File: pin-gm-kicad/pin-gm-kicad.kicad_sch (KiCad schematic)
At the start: 37 parts

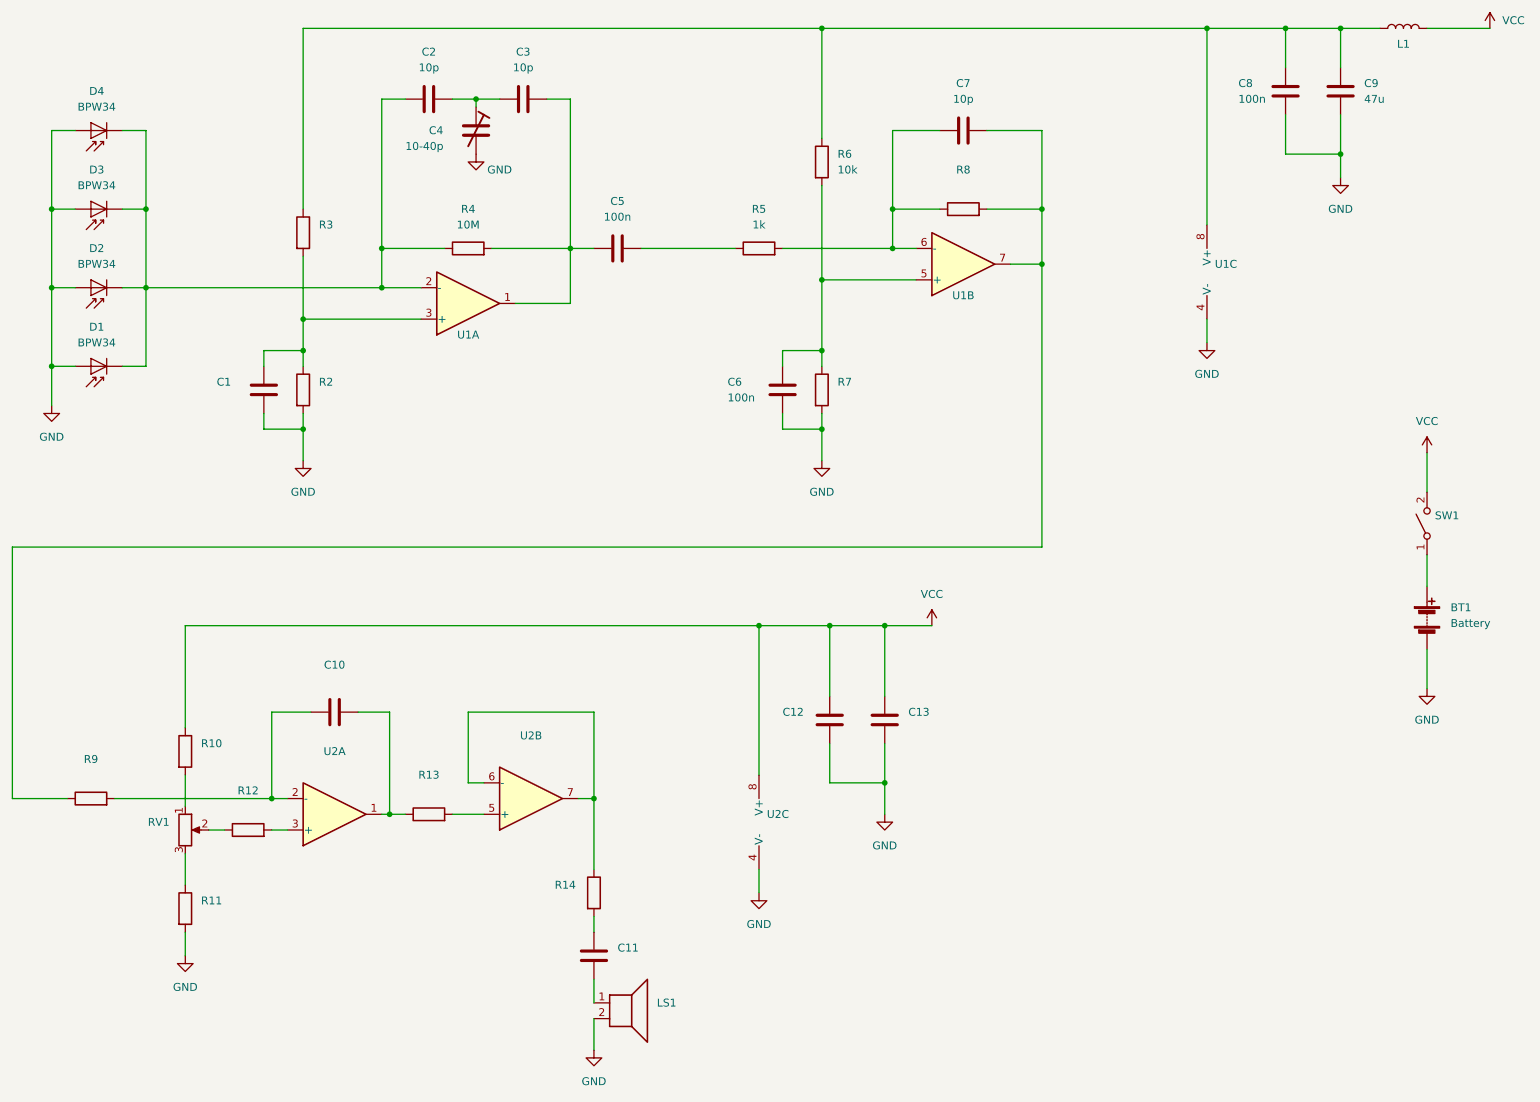
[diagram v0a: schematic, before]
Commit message: trimmer kondi footprint kezdemény
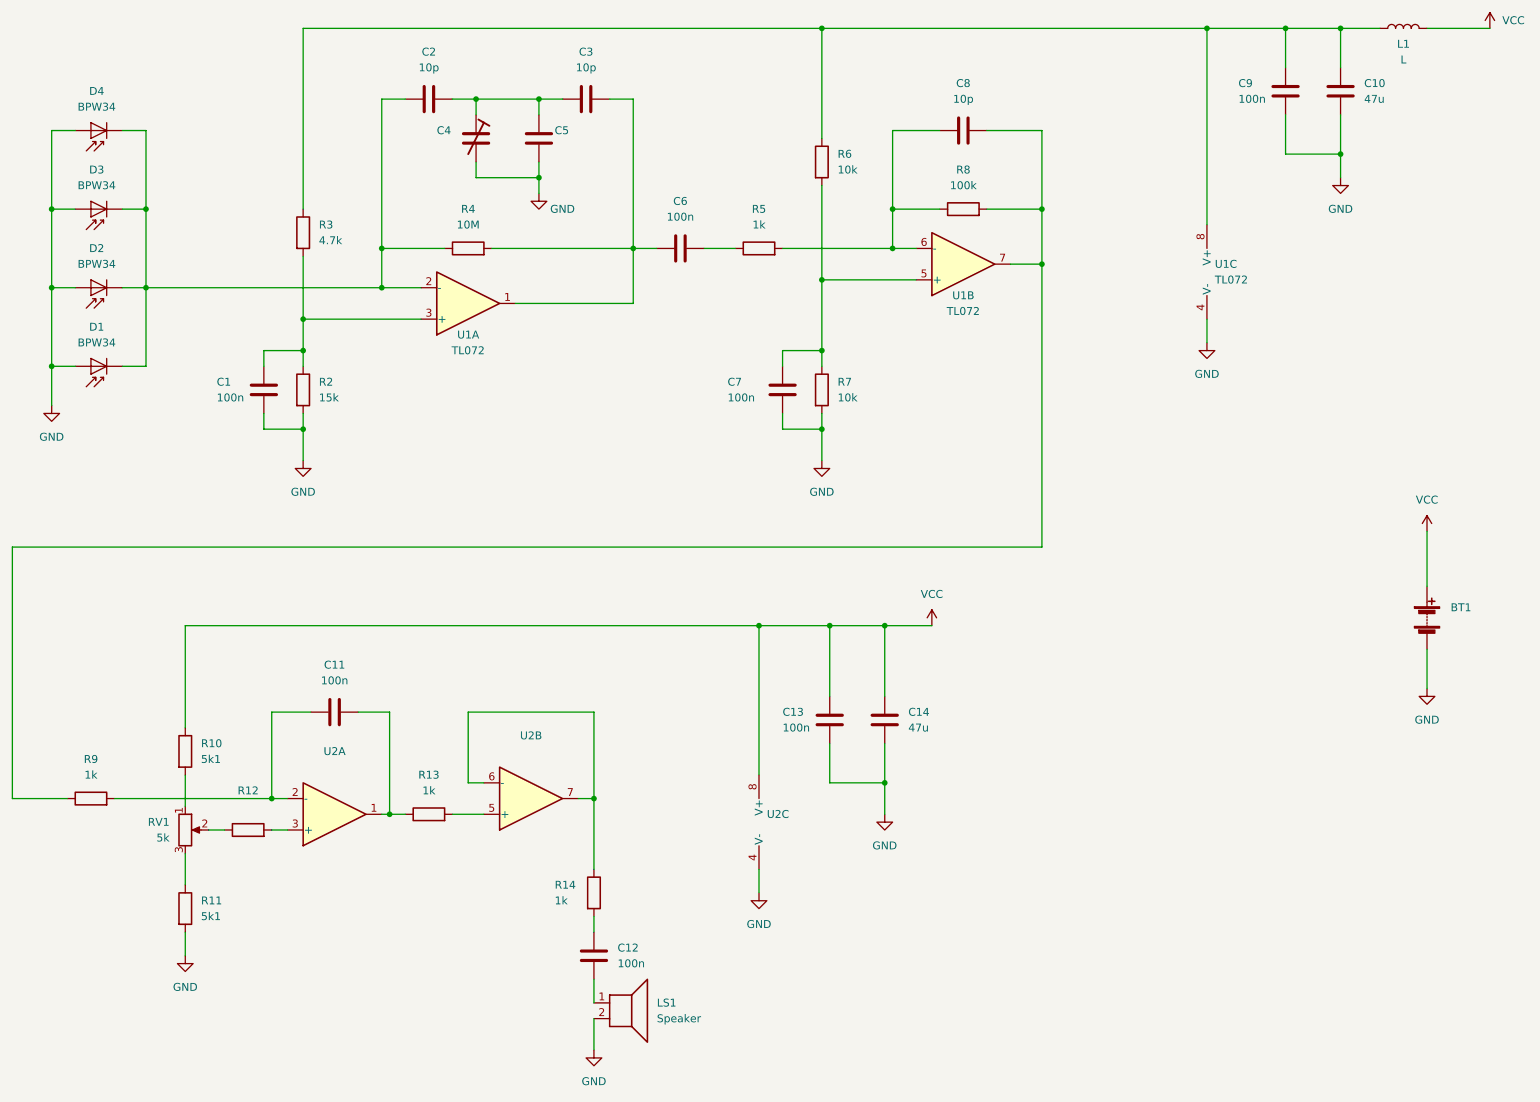
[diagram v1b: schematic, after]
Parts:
- removed SW1: (no value), symbol Switch:SW_SPST
- added C5: (no value), symbol Device:C
- BT1: value Battery -> (none)
- C1: value (none) -> 100n; footprint (none) -> Capacitor_SMD:C_1206_3216Metric_Pad1.33x1.80mm_HandSolder
- C10: renamed from C9; footprint (none) -> Capacitor_SMD:C_1210_3225Metric_Pad1.33x2.70mm_HandSolder
- C11: renamed from C10; value (none) -> 100n; footprint (none) -> Capacitor_SMD:C_1206_3216Metric_Pad1.33x1.80mm_HandSolder
- C12: renamed from C11; value (none) -> 100n; footprint (none) -> Capacitor_SMD:C_1206_3216Metric_Pad1.33x1.80mm_HandSolder
- C13: renamed from C12; value (none) -> 100n; footprint (none) -> Capacitor_SMD:C_1206_3216Metric_Pad1.33x1.80mm_HandSolder
- C14: renamed from C13; value (none) -> 47u; footprint (none) -> Capacitor_SMD:C_1210_3225Metric_Pad1.33x2.70mm_HandSolder
- C2, C3: footprint (none) -> Capacitor_SMD:C_1206_3216Metric_Pad1.33x1.80mm_HandSolder
- C4: value 10-40p -> (none)
- C6: renamed from C5; footprint (none) -> Capacitor_SMD:C_1206_3216Metric_Pad1.33x1.80mm_HandSolder
- C7: renamed from C6; footprint (none) -> Capacitor_SMD:C_1206_3216Metric_Pad1.33x1.80mm_HandSolder
- C8: renamed from C7; footprint (none) -> Capacitor_SMD:C_1206_3216Metric_Pad1.33x1.80mm_HandSolder
- C9: renamed from C8; footprint (none) -> Capacitor_SMD:C_1206_3216Metric_Pad1.33x1.80mm_HandSolder
- L1: value (none) -> L; footprint (none) -> Inductor_SMD:L_Bourns_SRR0604_homemade
- LS1: value (none) -> Speaker; footprint (none) -> Connector_Wire:SolderWire-2sqmm_1x02_P7.8mm_D2mm_OD3.9mm
- R10, R11: value (none) -> 5k1; footprint (none) -> Resistor_SMD:R_1206_3216Metric_Pad1.30x1.75mm_HandSolder
- R13, R9: value (none) -> 1k; footprint (none) -> Resistor_SMD:R_1206_3216Metric_Pad1.30x1.75mm_HandSolder
- R14: value (none) -> 1k; footprint (none) -> Resistor_SMD:R_1206_3216Metric
- R2: value (none) -> 15k; footprint (none) -> Resistor_SMD:R_1206_3216Metric_Pad1.30x1.75mm_HandSolder
- R3: value (none) -> 4.7k; footprint (none) -> Resistor_SMD:R_1206_3216Metric_Pad1.30x1.75mm_HandSolder
- R4, R5, R6: footprint (none) -> Resistor_SMD:R_1206_3216Metric_Pad1.30x1.75mm_HandSolder
- R7: value (none) -> 10k; footprint (none) -> Resistor_SMD:R_1206_3216Metric_Pad1.30x1.75mm_HandSolder
- R8: value (none) -> 100k; footprint (none) -> Resistor_SMD:R_1206_3216Metric_Pad1.30x1.75mm_HandSolder
- RV1: value (none) -> 5k; footprint (none) -> Potentiometer_THT:Potentiometer_Piher_PT-10-V10_Vertical
- U1: value (none) -> TL072; footprint (none) -> Package_SO:SO-8_3.9x4.9mm_P1.27mm
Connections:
- net GND: now also C5.2
- net VCC: now also BT1.1 (+)
- net at C2.2, C3.1, C4.1: now also C5.1
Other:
- moved on the sheet: C3, C4, C6

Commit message: kb semmi
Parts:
- C1: value 100n -> (none); footprint Capacitor_SMD:C_1206_3216Metric_Pad1.33x1.80mm_HandSolder -> (none)
- C10: renamed from C13; value 100n -> (none); footprint Capacitor_SMD:C_1206_3216Metric_Pad1.33x1.80mm_HandSolder -> (none)
- C11: renamed from C14; value 47u -> (none); footprint Capacitor_SMD:C_1210_3225Metric_Pad1.33x2.70mm_HandSolder -> (none)
- C12: renamed from C8; value 10p -> (none); footprint Capacitor_SMD:C_1206_3216Metric_Pad1.33x1.80mm_HandSolder -> (none)
- C13: renamed from C9; value 100n -> (none); footprint Capacitor_SMD:C_1206_3216Metric_Pad1.33x1.80mm_HandSolder -> (none)
- C14: renamed from C10; value 47u -> (none); footprint Capacitor_SMD:C_1210_3225Metric_Pad1.33x2.70mm_HandSolder -> (none)
- C2: renamed from C11; value 100n -> (none); footprint Capacitor_SMD:C_1206_3216Metric_Pad1.33x1.80mm_HandSolder -> (none)
- C3: renamed from C2; value 10p -> (none); footprint Capacitor_SMD:C_1206_3216Metric_Pad1.33x1.80mm_HandSolder -> (none)
- C6: renamed from C3; value 10p -> (none); footprint Capacitor_SMD:C_1206_3216Metric_Pad1.33x1.80mm_HandSolder -> (none)
- C7: renamed from C12; value 100n -> (none); footprint Capacitor_SMD:C_1206_3216Metric_Pad1.33x1.80mm_HandSolder -> (none)
- C8: renamed from C6; value 100n -> (none); footprint Capacitor_SMD:C_1206_3216Metric_Pad1.33x1.80mm_HandSolder -> (none)
- C9: renamed from C7; value 100n -> (none); footprint Capacitor_SMD:C_1206_3216Metric_Pad1.33x1.80mm_HandSolder -> (none)
- D1: renamed from D4; value BPW34 -> (none); footprint OptoDevice:Osram_DIL2_4.3x4.65mm_P5.08mm -> (none)
- D2: renamed from D3; value BPW34 -> (none); footprint OptoDevice:Osram_DIL2_4.3x4.65mm_P5.08mm -> (none)
- D3: renamed from D2; value BPW34 -> (none); footprint OptoDevice:Osram_DIL2_4.3x4.65mm_P5.08mm -> (none)
- D4: renamed from D1; value BPW34 -> (none); footprint OptoDevice:Osram_DIL2_4.3x4.65mm_P5.08mm -> (none)
- L1: value L -> (none); footprint Inductor_SMD:L_Bourns_SRR0604_homemade -> (none)
- LS1: value Speaker -> (none); footprint Connector_Wire:SolderWire-2sqmm_1x02_P7.8mm_D2mm_OD3.9mm -> (none)
- R1: renamed from R9; value 1k -> (none); footprint Resistor_SMD:R_1206_3216Metric_Pad1.30x1.75mm_HandSolder -> (none)
- R10: renamed from R5; value 1k -> (none); footprint Resistor_SMD:R_1206_3216Metric_Pad1.30x1.75mm_HandSolder -> (none)
- R11: renamed from R6; value 10k -> (none); footprint Resistor_SMD:R_1206_3216Metric_Pad1.30x1.75mm_HandSolder -> (none)
- R12: renamed from R7; value 10k -> (none); footprint Resistor_SMD:R_1206_3216Metric_Pad1.30x1.75mm_HandSolder -> (none)
- R13: renamed from R8; value 100k -> (none); footprint Resistor_SMD:R_1206_3216Metric_Pad1.30x1.75mm_HandSolder -> (none)
- R2: renamed from R10; value 5k1 -> (none); footprint Resistor_SMD:R_1206_3216Metric_Pad1.30x1.75mm_HandSolder -> (none)
- R3: renamed from R11; value 5k1 -> (none); footprint Resistor_SMD:R_1206_3216Metric_Pad1.30x1.75mm_HandSolder -> (none)
- R5: renamed from R3; value 4.7k -> (none); footprint Resistor_SMD:R_1206_3216Metric_Pad1.30x1.75mm_HandSolder -> (none)
- R6: renamed from R2; value 15k -> (none); footprint Resistor_SMD:R_1206_3216Metric_Pad1.30x1.75mm_HandSolder -> (none)
- R7: renamed from R13; value 1k -> (none); footprint Resistor_SMD:R_1206_3216Metric_Pad1.30x1.75mm_HandSolder -> (none)
- R8: renamed from R4; value 10M -> (none); footprint Resistor_SMD:R_1206_3216Metric_Pad1.30x1.75mm_HandSolder -> (none)
- R9: renamed from R14; value 1k -> (none); footprint Resistor_SMD:R_1206_3216Metric -> (none)
- RV1: value 5k -> (none); footprint Potentiometer_THT:Potentiometer_Piher_PT-10-V10_Vertical -> (none)
- U2: renamed from U1; value TL072 -> (none); footprint Package_SO:SO-8_3.9x4.9mm_P1.27mm -> (none)
- renumbered R12 to R4, U2 to U1

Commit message: kész vannak a footprintek
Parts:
- added C7: (no value), symbol Device:C
- renumbered C9 to C10, C10 to C11, C11 to C12, C12 to C13, C13 to C14, C14 to C15, C7 to C6, C6 to C8, C8 to C9
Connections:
- net GND: now also C7.2
- net at C8.2, C9.1: no longer R8.2, U2.1
- net Diode_Cathode: now reaches C3.1, D1.1 (K), D2.1 (K), D3.1 (K), D4.1 (K), R8.1, U2.2 (-)
- net at C3.2, C4.1, C5.1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: now also C7.1
- new net: R8.2, U2.1
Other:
- moved on the sheet: C8, C9, R10

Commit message: kis haladás
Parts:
- BT1: value (none) -> Battery; footprint (none) -> Homemade:SolderWire-homemade
- C1, C10, C11, C14, C2, C6, C9: value (none) -> 100n; footprint (none) -> Homemade:C_1206_3216Metric_homemade
- C12, C15: value (none) -> 47u; footprint (none) -> Homemade:C_1210_3225Metric_homemade
- C13, C3, C5, C7, C8: value (none) -> 10p; footprint (none) -> Homemade:C_1206_3216Metric_homemade
- C4: value (none) -> 10-40p; footprint (none) -> Homemade:C_trimmer_D10mm_homemade
- D1, D2, D4: value (none) -> BPW34; footprint (none) -> Homemade:BPW34_homemade
- L1: value (none) -> 1m; footprint (none) -> Homemade:L_Bourns_SRR0604_homemade
- LS1: value (none) -> Speaker; footprint (none) -> Homemade:SolderWire-homemade
- R1, R10, R4, R7, R9: value (none) -> 1k; footprint (none) -> Homemade:R_1206_3216Metric_homemade
- R11, R12: value (none) -> 10k; footprint (none) -> Homemade:R_1206_3216Metric_homemade
- R13: value (none) -> 100k; footprint (none) -> Homemade:R_1206_3216Metric_homemade
- R2, R3: value (none) -> 5k1; footprint (none) -> Homemade:R_1206_3216Metric_homemade
- R5: value (none) -> 4.7k; footprint (none) -> Homemade:R_1206_3216Metric_homemade
- R6: value (none) -> 15k; footprint (none) -> Homemade:R_1206_3216Metric_homemade
- R8: value (none) -> 10M; footprint (none) -> Homemade:R_1206_3216Metric_homemade
- RV1: value (none) -> 5k; footprint (none) -> Homemade:Potentiometer_D10_vert_homemade
- U1: value (none) -> LM358; footprint (none) -> Homemade:SO-8_3.9x4.9mm_homemade
- U2: value (none) -> TL072; footprint (none) -> Homemade:SO-8_3.9x4.9mm_homemade

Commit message: kb elhelyezve
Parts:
- added H1, H2: (no value), symbol Mechanical:MountingHole_Pad
- BT1: value Battery -> (none); footprint Homemade:SolderWire-homemade -> (none)
- C1, C10, C11, C14, C2, C6, C9: value 100n -> (none); footprint Homemade:C_1206_3216Metric_homemade -> (none)
- C12, C15: value 47u -> (none); footprint Homemade:C_1210_3225Metric_homemade -> (none)
- C13, C3, C5, C7, C8: value 10p -> (none); footprint Homemade:C_1206_3216Metric_homemade -> (none)
- C4: value 10-40p -> (none); footprint Homemade:C_trimmer_D10mm_homemade -> (none)
- D1, D2, D4: value BPW34 -> (none); footprint Homemade:BPW34_homemade -> (none)
- L1: value 1m -> (none); footprint Homemade:L_Bourns_SRR0604_homemade -> (none)
- LS1: value Speaker -> (none); footprint Homemade:SolderWire-homemade -> (none)
- R1, R10, R4, R7, R9: value 1k -> (none); footprint Homemade:R_1206_3216Metric_homemade -> (none)
- R11, R12: value 10k -> (none); footprint Homemade:R_1206_3216Metric_homemade -> (none)
- R13: value 100k -> (none); footprint Homemade:R_1206_3216Metric_homemade -> (none)
- R2, R3: value 5k1 -> (none); footprint Homemade:R_1206_3216Metric_homemade -> (none)
- R5: value 4.7k -> (none); footprint Homemade:R_1206_3216Metric_homemade -> (none)
- R6: value 15k -> (none); footprint Homemade:R_1206_3216Metric_homemade -> (none)
- R8: value 10M -> (none); footprint Homemade:R_1206_3216Metric_homemade -> (none)
- RV1: value 5k -> (none); footprint Homemade:Potentiometer_D10_vert_homemade -> (none)
- U1: value LM358 -> (none); footprint Homemade:SO-8_3.9x4.9mm_homemade -> (none)
- U2: value TL072 -> (none); footprint Homemade:SO-8_3.9x4.9mm_homemade -> (none)
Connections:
- net GND: now also H1.1, H2.1
- net at C8.2, C9.1: now also R8.2, U2.1
